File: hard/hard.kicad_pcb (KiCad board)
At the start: 2 copper layers, 125 parts, among them U1 STM32F401RETx, U2 USBLC6-2SC6, U3 AMS1117-3.3

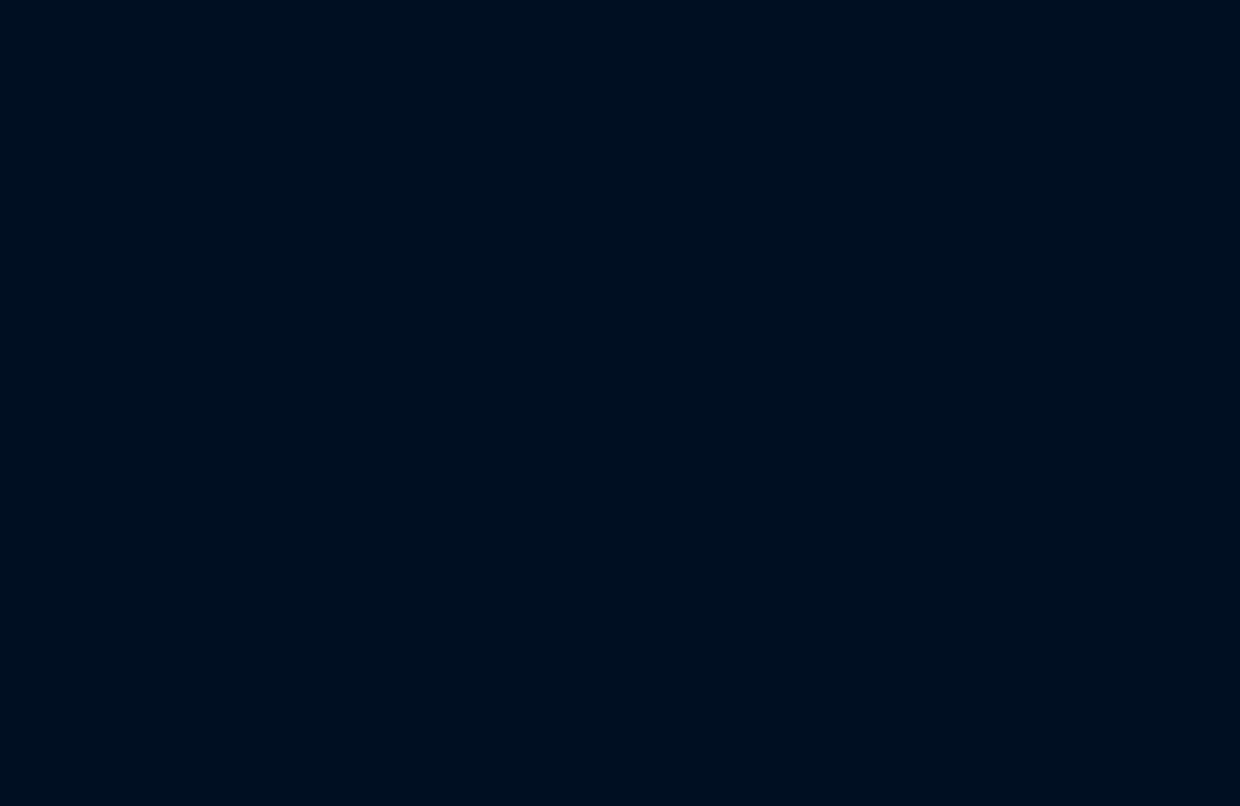
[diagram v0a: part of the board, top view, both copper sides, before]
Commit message: assign all footprints
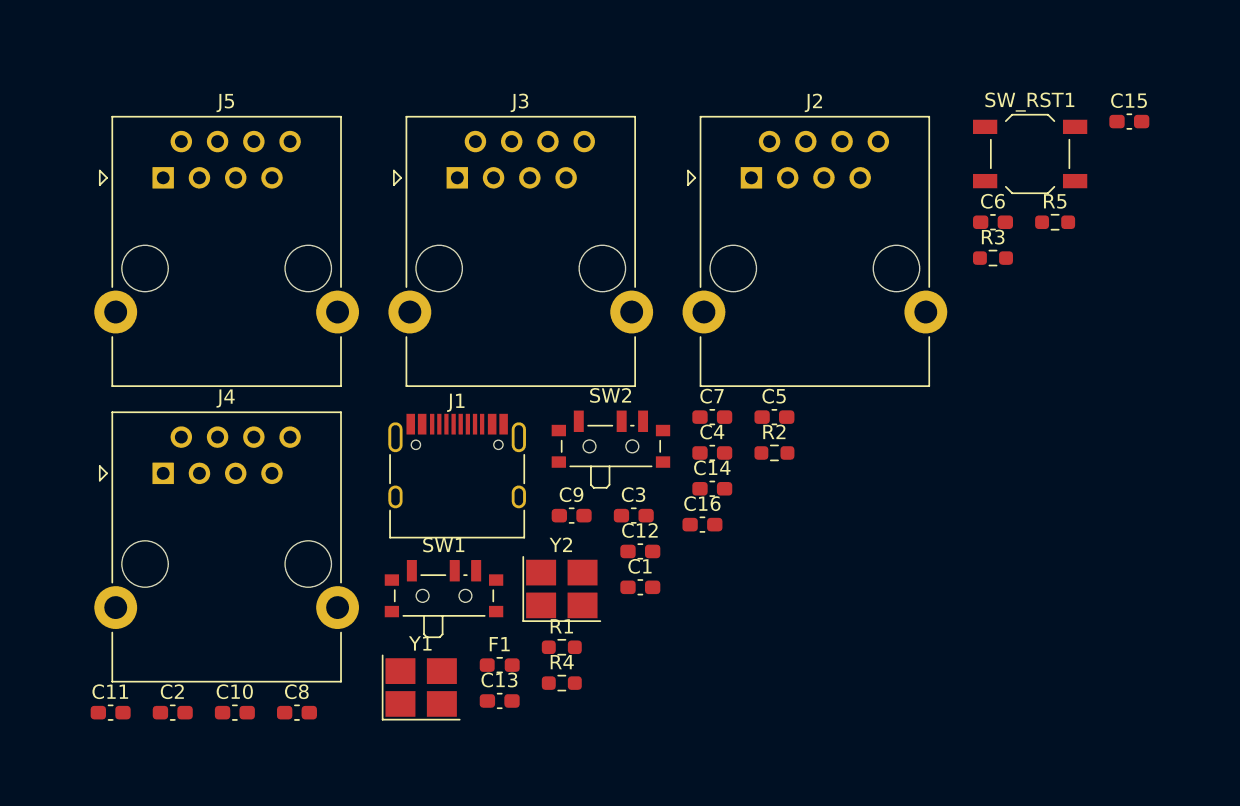
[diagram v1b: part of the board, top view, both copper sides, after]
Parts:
- added C1: 12pF, Capacitor_SMD:C_0603_1608Metric_Pad1.08x0.95mm_HandSolder, F.Cu at (949.3, -151.8)
- added C10: 0.1uF, Capacitor_SMD:C_0603_1608Metric_Pad1.08x0.95mm_HandSolder, F.Cu at (920.9, -143.0)
- added C11: 0.1uF, Capacitor_SMD:C_0603_1608Metric_Pad1.08x0.95mm_HandSolder, F.Cu at (912.2, -143.0)
- added C12: 0.1uF, Capacitor_SMD:C_0603_1608Metric_Pad1.08x0.95mm_HandSolder, F.Cu at (949.3, -154.3)
- added C13: 10uF, Capacitor_SMD:C_0603_1608Metric_Pad1.08x0.95mm_HandSolder, F.Cu at (939.5, -143.8)
- added C14: 0.1uF, Capacitor_SMD:C_0603_1608Metric_Pad1.08x0.95mm_HandSolder, F.Cu at (954.4, -158.7)
- added C15: 0.1uF, Capacitor_SMD:C_0603_1608Metric_Pad1.08x0.95mm_HandSolder, F.Cu at (983.6, -184.4)
- added C16: 10uF, Capacitor_SMD:C_0603_1608Metric_Pad1.08x0.95mm_HandSolder, F.Cu at (953.7, -156.2)
- added C2: 12pF, Capacitor_SMD:C_0603_1608Metric_Pad1.08x0.95mm_HandSolder, F.Cu at (916.6, -143.0)
- added C3: 12pF, Capacitor_SMD:C_0603_1608Metric_Pad1.08x0.95mm_HandSolder, F.Cu at (948.9, -156.8)
- added C4: 12pF, Capacitor_SMD:C_0603_1608Metric_Pad1.08x0.95mm_HandSolder, F.Cu at (954.4, -161.2)
- added C5: 0.1uF, Capacitor_SMD:C_0603_1608Metric_Pad1.08x0.95mm_HandSolder, F.Cu at (958.7, -163.7)
- added C6: 4.7uF, Capacitor_SMD:C_0603_1608Metric_Pad1.08x0.95mm_HandSolder, F.Cu at (974.0, -177.3)
- added C7: 0.1uF, Capacitor_SMD:C_0603_1608Metric_Pad1.08x0.95mm_HandSolder, F.Cu at (954.4, -163.7)
- added C8: 0.1uF, Capacitor_SMD:C_0603_1608Metric_Pad1.08x0.95mm_HandSolder, F.Cu at (925.3, -143.0)
- added C9: 0.1uF, Capacitor_SMD:C_0603_1608Metric_Pad1.08x0.95mm_HandSolder, F.Cu at (944.5, -156.8)
- added F1: Polyfuse, Fuse:Fuse_0603_1608Metric_Pad1.05x0.95mm_HandSolder, F.Cu at (939.5, -146.3)
- added J1: USB_C_Receptacle_USB2.0, Connector_USB:USB_C_Receptacle_HRO_TYPE-C-31-M-12, F.Cu at (936.5, -159.1)
- added J2: RJ45_Shielded, Connector_RJ:RJ45_Ninigi_GE, F.Cu at (957.1, -180.4)
- added J3: RJ45_Shielded, Connector_RJ:RJ45_Ninigi_GE, F.Cu at (936.5, -180.4)
- added J4: RJ45_Shielded, Connector_RJ:RJ45_Ninigi_GE, F.Cu at (915.9, -159.7)
- added J5: RJ45_Shielded, Connector_RJ:RJ45_Ninigi_GE, F.Cu at (915.9, -180.4)
- added R1: 10kohm, Resistor_SMD:R_0603_1608Metric_Pad0.98x0.95mm_HandSolder, F.Cu at (943.8, -147.6)
- added R2: 10kohm, Resistor_SMD:R_0603_1608Metric_Pad0.98x0.95mm_HandSolder, F.Cu at (958.7, -161.2)
- added R3: 4.7kohm, Resistor_SMD:R_0603_1608Metric_Pad0.98x0.95mm_HandSolder, F.Cu at (974.0, -174.8)
- added R4: 5.1kohm, Resistor_SMD:R_0603_1608Metric_Pad0.98x0.95mm_HandSolder, F.Cu at (943.8, -145.1)
- added R5: 5.1kohm, Resistor_SMD:R_0603_1608Metric_Pad0.98x0.95mm_HandSolder, F.Cu at (978.4, -177.3)
- added SW1: BOOT0, Button_Switch_SMD:SW_SPDT_PCM12, F.Cu at (935.6, -151.5)
- added SW2: BOOT1, Button_Switch_SMD:SW_SPDT_PCM12, F.Cu at (947.3, -162.0)
- added SW_RST1: RST, Button_Switch_SMD:SW_SPST_TL3342, F.Cu at (976.6, -182.1)
- added Y1: XTAL_8M, Crystal:Crystal_SMD_3225-4Pin_3.2x2.5mm_HandSoldering, F.Cu at (934.0, -144.7)
- added Y2: XTAL_8M, Crystal:Crystal_SMD_3225-4Pin_3.2x2.5mm_HandSoldering, F.Cu at (943.8, -151.6)
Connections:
- D62 pad 1: (no net) -> /COL7L
- U1 pad 28: (no net) -> /BOOT1
- U1 pad 3: (no net) -> /XTAL_32K_A
- U1 pad 30: (no net) -> Net-(C6-Pad1)
- U1 pad 4: (no net) -> /XTAL_32K_B
- U1 pad 60: (no net) -> /BOOT0
- U1 pad 7: (no net) -> Net-(R3-Pad2)
- U2 pad 4: (no net) -> Net-(J1-PadA7)
- U2 pad 6: (no net) -> Net-(J1-PadA6)
- U3 pad 3: (no net) -> Net-(C13-Pad1)

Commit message: draw outline
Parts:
- removed J4, J5: RJ45_Shielded, Connector_RJ:RJ45_Ninigi_GE
- added C17: 0.1uF, Capacitor_SMD:C_0603_1608Metric_Pad1.08x0.95mm_HandSolder, F.Cu at (1061.7, -113.0)
- added C18: 4.7uF, Capacitor_SMD:C_0603_1608Metric_Pad1.08x0.95mm_HandSolder, F.Cu at (1061.7, -110.5)
- added C19: 0.1uF, Capacitor_SMD:C_0603_1608Metric_Pad1.08x0.95mm_HandSolder, F.Cu at (1066.1, -113.0)
- added C20: 0.1uF, Capacitor_SMD:C_0603_1608Metric_Pad1.08x0.95mm_HandSolder, F.Cu at (1061.7, -108.0)
- added C21: 0.1uF, Capacitor_SMD:C_0603_1608Metric_Pad1.08x0.95mm_HandSolder, F.Cu at (1066.1, -110.5)
- added C22: 0.1uF, Capacitor_SMD:C_0603_1608Metric_Pad1.08x0.95mm_HandSolder, F.Cu at (1070.4, -113.0)
- added C23: 0.1uF, Capacitor_SMD:C_0603_1608Metric_Pad1.08x0.95mm_HandSolder, F.Cu at (1066.1, -108.0)
- added C24: 12pF, Capacitor_SMD:C_0603_1608Metric_Pad1.08x0.95mm_HandSolder, F.Cu at (1096.6, -132.7)
- added C25: 12pF, Capacitor_SMD:C_0603_1608Metric_Pad1.08x0.95mm_HandSolder, F.Cu at (1090.2, -125.8)
- added C26: 12pF, Capacitor_SMD:C_0603_1608Metric_Pad1.08x0.95mm_HandSolder, F.Cu at (1096.6, -130.2)
- added C27: 12pF, Capacitor_SMD:C_0603_1608Metric_Pad1.08x0.95mm_HandSolder, F.Cu at (1090.2, -123.3)
- added R6: 4.7kohm, Resistor_SMD:R_0603_1608Metric_Pad0.98x0.95mm_HandSolder, F.Cu at (1070.4, -110.5)
- added R7: 10kohm, Resistor_SMD:R_0603_1608Metric_Pad0.98x0.95mm_HandSolder, F.Cu at (1094.6, -125.8)
- added R8: 10kohm, Resistor_SMD:R_0603_1608Metric_Pad0.98x0.95mm_HandSolder, F.Cu at (1094.6, -123.3)
- added SW3: BOOT0, Button_Switch_SMD:SW_SPDT_PCM12, F.Cu at (1005.2, -87.6)
- added SW4: BOOT1, Button_Switch_SMD:SW_SPDT_PCM12, F.Cu at (1015.4, -87.6)
- added SW_RST2: RST, Button_Switch_SMD:SW_SPST_TL3342, F.Cu at (1048.4, -86.4)
- added U4: STM32F401RETx, Package_QFP:LQFP-64_10x10mm_P0.5mm, F.Cu at (1033.1, -80.6)
- added Y3: XTAL_8M, Crystal:Crystal_SMD_3225-4Pin_3.2x2.5mm_HandSoldering, F.Cu at (1078.1, -124.2)
- added Y4: XTAL_8M, Crystal:Crystal_SMD_3225-4Pin_3.2x2.5mm_HandSoldering, F.Cu at (1084.7, -124.2)
- SW_BS1: footprint hard:Kailh_Choc_V2_1.00u_PCB -> hard:Kailh_Choc_V2_1.50u_PCB
- moved U1 223.2 mm to (857.9, -81.9)
- moved SW_RST1 164.2 mm to (843.3, -86.4)
- moved J3 119.8 mm to (993.1, -74.9), turned to 180 degrees
- moved J2 113.4 mm to (915.7, -74.9), turned to 180 degrees
- moved SW2 97.7 mm to (883.9, -87.6), turned to 180 degrees
- moved D4 91.4 mm to (1016.4, -102.5)
- moved D10 91.4 mm to (1026.8, -114.4)
- moved D13 91.4 mm to (1008.8, -96.8)
- moved D15 91.4 mm to (1026.8, -117.0)
- moved D5 91.4 mm to (1026.8, -111.8)
- moved D11 91.4 mm to (1012.4, -99.9)
- moved D14 91.4 mm to (1012.4, -102.5)
- moved SW1 88.6 mm to (874.2, -87.6), turned to 180 degrees
- moved J1 84.5 mm to (894.7, -85.7), turned to 180 degrees
- moved D20 72.1 mm to (900.2, -149.4)
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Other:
- board outline added: 315.6 x 117.5 mm

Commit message: set all footprints
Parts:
- removed C26, C27, C3, C4: 12pF, Capacitor_SMD:C_0603_1608Metric_Pad1.08x0.95mm_HandSolder
- removed Y2, Y4: XTAL_8M, Crystal:Crystal_SMD_3225-4Pin_3.2x2.5mm_HandSoldering
- added REF**: MountingHole_2.2mm_M2, MountingHole:MountingHole_2.2mm_M2, F.Cu at (1037.6, -72.3)
- added REF**: MountingHole_2.2mm_M2, MountingHole:MountingHole_2.2mm_M2, F.Cu at (1037.6, -87.5)
- added REF**: MountingHole_2.2mm_M2, MountingHole:MountingHole_2.2mm_M2, F.Cu at (1001.4, -82.4)
- added REF**: MountingHole_2.2mm_M2, MountingHole:MountingHole_2.2mm_M2, F.Cu at (1001.4, -72.4)
- added REF**: MountingHole_2.2mm_M2, MountingHole:MountingHole_2.2mm_M2, F.Cu at (886.5, -72.5)
- added REF**: MountingHole_2.2mm_M2, MountingHole:MountingHole_2.2mm_M2, F.Cu at (886.5, -82.5)
- added REF**: MountingHole_2.2mm_M2, MountingHole:MountingHole_2.2mm_M2, F.Cu at (850.3, -72.5)
- added REF**: MountingHole_2.2mm_M2, MountingHole:MountingHole_2.2mm_M2, F.Cu at (850.3, -87.8)
- moved D61 239.2 mm to (1100.0, -10.2)
- moved D58 229.8 mm to (1106.2, -68.6)
- moved D36 227.3 mm to (996.3, 7.62)
- moved D49 217.3 mm to (1044.6, -10.8)
- moved D53 216.8 mm to (1054.1, -29.8)
- moved D4 214.7 mm to (822.3, -10.8)
- moved D60 212.9 mm to (1078.2, -29.2)
- moved D59 210.5 mm to (1085.8, -49.5)
- moved D52 206.6 mm to (1049.7, -48.9)
- moved D57 205.0 mm to (1062.4, -10.8)
- moved C22 204.9 mm to (869.3, -73.7), turned to 90 degrees
- moved D35 204.8 mm to (987.4, -11.4)
- moved D48 203.0 mm to (1035.0, -30.5)
- moved D5 202.3 mm to (829.3, -67.9)
- moved D56 201.9 mm to (1077.0, -67.3)
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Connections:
- C1 pad 1: /XTAL_8M_B -> /L_XTAL_8M_B
- C2 pad 1: /XTAL_8M_A -> /L_XTAL_8M_A
- C24 pad 1: /XTAL_8M_B -> /R_XTAL_8M_B
- C25 pad 1: /XTAL_8M_A -> /R_XTAL_8M_A
- D62 pad 1: /COL7L -> (no net)
- J2 pad 4: /ROW5L -> (no net)
- J2 pad 5: /ROW4L -> (no net)
- J2 pad 6: /ROW3L -> (no net)
- J2 pad 7: /ROW2L -> (no net)
- J2 pad 8: /ROW1L -> (no net)
- J3 pad 2: /COL7L -> (no net)
- J3 pad 3: /COL6L -> (no net)
- J3 pad 4: /COL5L -> (no net)
- J3 pad 5: /COL4L -> (no net)
- J3 pad 6: /COL3L -> (no net)
- J3 pad 7: /COL2L -> (no net)
- J3 pad 8: /COL1L -> (no net)
- R1 pad 1: /BOOT0 -> /R_BOOT0
- R2 pad 1: /BOOT1 -> /R_BOOT1
- R7 pad 1: /BOOT0 -> /L_BOOT0
- R8 pad 1: /BOOT1 -> /L_BOOT1
- SW1 pad 2: /BOOT0 -> /R_BOOT0
- SW2 pad 2: /BOOT1 -> /R_BOOT1
- SW3 pad 2: /BOOT0 -> /L_BOOT0
- SW4 pad 2: /BOOT1 -> /L_BOOT1
- U1 pad 28: /BOOT1 -> /L_BOOT1
- U1 pad 3: /XTAL_32K_A -> (no net)
- U1 pad 4: /XTAL_32K_B -> (no net)
- U1 pad 5: /XTAL_8M_A -> /L_XTAL_8M_A
- U1 pad 6: /XTAL_8M_A -> /L_XTAL_8M_B
- U1 pad 60: /BOOT0 -> /L_BOOT0
- U4 pad 28: /BOOT1 -> /R_BOOT1
- U4 pad 3: /XTAL_32K_A -> (no net)
- U4 pad 4: /XTAL_32K_B -> (no net)
- U4 pad 5: /XTAL_8M_A -> /R_XTAL_8M_A
- U4 pad 6: /XTAL_8M_A -> /R_XTAL_8M_B
- U4 pad 60: /BOOT0 -> /R_BOOT0
- Y1 pad 1: /XTAL_8M_B -> /L_XTAL_8M_B
- Y1 pad 3: /XTAL_8M_A -> /L_XTAL_8M_A
- Y3 pad 1: /XTAL_8M_B -> /R_XTAL_8M_B
- Y3 pad 3: /XTAL_8M_A -> /R_XTAL_8M_A
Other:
- outline, holes or cut-outs redrawn

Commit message: misc circuits
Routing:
- net +3V3: track 0.00 -> 2.33 mm
- net GND: track 0.00 -> 2.07 mm

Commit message: gen2
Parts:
- removed C15, C17, C19, C20, C21, C22, C23: 0.1uF, Capacitor_SMD:C_0603_1608Metric_Pad1.08x0.95mm_HandSolder
- removed C16: 10uF, Capacitor_SMD:C_0603_1608Metric_Pad1.08x0.95mm_HandSolder
- removed C18: 4.7uF, Capacitor_SMD:C_0603_1608Metric_Pad1.08x0.95mm_HandSolder
- removed C24, C25: 12pF, Capacitor_SMD:C_0603_1608Metric_Pad1.08x0.95mm_HandSolder
- removed D10, D11, D12, D13, D14, D15, D16, D17, D18, D19, D20, D21, D22, D23, D24, D25, D26, D27, D29, D30, D31, D32, D33, D34, D35, D36, D37, D38, D39, D4, D40, D41, D42, D43, D44, D45, D46, D47, D48, D49, D5, D50, D51, D52, D53, D54, D55, D56, D57, D58, D59, D6, D60, D61, D62, D7, D8, D9: D, Diode_SMD:D_0603_1608Metric
- removed J3: RJ45_Shielded, Connector_RJ:RJ45_Ninigi_GE
- removed REF** (x8): MountingHole_2.2mm_M2, MountingHole:MountingHole_2.2mm_M2
- removed SW_0: SW_0, hard:Kailh_Choc_V2_1.00u_PCB
- removed SW_1: SW_1, hard:Kailh_Choc_V2_1.00u_PCB
- removed SW_10: SW_6, hard:Kailh_Choc_V2_1.00u_PCB
- removed SW_2: SW_2, hard:Kailh_Choc_V2_1.00u_PCB
- removed SW_3: SW_3, hard:Kailh_Choc_V2_1.00u_PCB
- removed SW_4: SW_4, hard:Kailh_Choc_V2_1.00u_PCB
- removed SW_5: SW_5, hard:Kailh_Choc_V2_1.00u_PCB
- removed SW_7: SW_7, hard:Kailh_Choc_V2_1.00u_PCB
- removed SW_8: SW_8, hard:Kailh_Choc_V2_1.00u_PCB
- removed SW_9: SW_9, hard:Kailh_Choc_V2_1.00u_PCB
- removed SW_A1: SW_A, hard:Kailh_Choc_V2_1.00u_PCB
- removed SW_B1: SW_B, hard:Kailh_Choc_V2_1.00u_PCB
- removed SW_BQ1: SW_BQ, hard:Kailh_Choc_V2_1.00u_PCB
- removed SW_BS1: SW_BS, hard:Kailh_Choc_V2_1.50u_PCB
- removed SW_C1: SW_C, hard:Kailh_Choc_V2_1.00u_PCB
- removed SW_CMM1: SW_CMM, hard:Kailh_Choc_V2_1.00u_PCB
- removed SW_CTRL1: SW_CTRL, hard:Kailh_Choc_V2_1.75u_PCB
- removed SW_D1: SW_D, hard:Kailh_Choc_V2_1.00u_PCB
- removed SW_DEL1: SW_DEL, hard:Kailh_Choc_V2_2.00u_PCB
- removed SW_E1: SW_E, hard:Kailh_Choc_V2_1.00u_PCB
- removed SW_ESC1: SW_ESC, hard:Kailh_Choc_V2_1.00u_PCB
- removed SW_F1: SW_F, hard:Kailh_Choc_V2_1.00u_PCB
- removed SW_FN1: SW_FN, hard:Kailh_Choc_V2_1.00u_PCB
- removed SW_G1: SW_G, hard:Kailh_Choc_V2_1.00u_PCB
- removed SW_H1: SW_H, hard:Kailh_Choc_V2_1.00u_PCB
- removed SW_HYPH1: SW_HYPH, hard:Kailh_Choc_V2_1.00u_PCB
- removed SW_I1: SW_I, hard:Kailh_Choc_V2_1.00u_PCB
- removed SW_J1: SW_J, hard:Kailh_Choc_V2_1.00u_PCB
- removed SW_K1: SW_K, hard:Kailh_Choc_V2_1.00u_PCB
- removed SW_L1: SW_L, hard:Kailh_Choc_V2_1.00u_PCB
- removed SW_LALT1: SW_LALT, hard:Kailh_Choc_V2_1.25u_PCB
- removed SW_LB1: SW_LB, hard:Kailh_Choc_V2_1.00u_PCB
- removed SW_LCMD1: SW_LCMD, hard:Kailh_Choc_V2_1.25u_PCB
- removed SW_LSFT1: SW_LSFT, hard:Kailh_Choc_V2_2.25u_PCB
- removed SW_LSPC1: SW_LSPC, hard:Kailh_Choc_V2_2.00u_PCB
- removed SW_M1: SW_M, hard:Kailh_Choc_V2_1.00u_PCB
- removed SW_N1: SW_N, hard:Kailh_Choc_V2_1.00u_PCB
- removed SW_O1: SW_O, hard:Kailh_Choc_V2_1.00u_PCB
- removed SW_P1: SW_P, hard:Kailh_Choc_V2_1.00u_PCB
- removed SW_PLUS1: SW_PLUS, hard:Kailh_Choc_V2_1.00u_PCB
- removed SW_PRD1: SW_PRD, hard:Kailh_Choc_V2_1.00u_PCB
- removed SW_Q1: SW_Q, hard:Kailh_Choc_V2_1.00u_PCB
- removed SW_R1: SW_R, hard:Kailh_Choc_V2_1.00u_PCB
- removed SW_RALT1: SW_RALT, hard:Kailh_Choc_V2_1.25u_PCB
- removed SW_RB1: SW_RB, hard:Kailh_Choc_V2_1.00u_PCB
- removed SW_RCMD1: SW_RCMD, hard:Kailh_Choc_V2_1.25u_PCB
- removed SW_RET1: SW_RET, hard:Kailh_Choc_V2_2.75u_PCB
- removed SW_RSFT1: SW_RSFT, hard:Kailh_Choc_V2_2.25u_PCB
- removed SW_RSPC1: SW_RSPC, hard:Kailh_Choc_V2_2.00u_PCB
- removed SW_RST1, SW_RST2: RST, Button_Switch_SMD:SW_SPST_TL3342
- removed SW_S1: SW_S, hard:Kailh_Choc_V2_1.00u_PCB
- removed SW_SEMI1: SW_SEMI, hard:Kailh_Choc_V2_1.00u_PCB
- removed SW_SLA1: SW_SLA, hard:Kailh_Choc_V2_1.00u_PCB
- removed SW_SQ1: SW_SQ, hard:Kailh_Choc_V2_1.00u_PCB
- removed SW_T1: SW_T, hard:Kailh_Choc_V2_1.00u_PCB
- removed SW_TAB1: SW_TAB, hard:Kailh_Choc_V2_1.50u_PCB
- removed SW_U1: SW_U, hard:Kailh_Choc_V2_1.00u_PCB
- removed SW_V1: SW_V, hard:Kailh_Choc_V2_1.00u_PCB
- removed SW_W1: SW_W, hard:Kailh_Choc_V2_1.00u_PCB
- removed SW_X1: SW_X, hard:Kailh_Choc_V2_1.00u_PCB
- removed SW_Y1: SW_Y, hard:Kailh_Choc_V2_1.00u_PCB
- removed SW_Z1: SW_Z, hard:Kailh_Choc_V2_1.00u_PCB
- removed Y3: XTAL_8M, Crystal:Crystal_SMD_3225-4Pin_3.2x2.5mm_HandSoldering
- added C3: 0.1uF, Capacitor_SMD:C_0402_1005Metric_Pad0.74x0.62mm_HandSolder, F.Cu at (175.8, 64.0)
- added C4: 0.1uF, Capacitor_SMD:C_0402_1005Metric_Pad0.74x0.62mm_HandSolder, F.Cu at (181.6, 63.0)
- added R10: 330Ohm, Resistor_SMD:R_0402_1005Metric_Pad0.72x0.64mm_HandSolder, F.Cu at (168.3, 45.7)
- added R9: 330Ohm, Resistor_SMD:R_0402_1005Metric_Pad0.72x0.64mm_HandSolder, F.Cu at (165.1, 46.4)
- added REF_M1: MountingHole_2.2mm_M2_DIN965, MountingHole:MountingHole_2.2mm_M2_DIN965, F.Cu at (188.0, 48.3)
- added REF_M2: MountingHole_2.2mm_M2_DIN965, MountingHole:MountingHole_2.2mm_M2_DIN965, F.Cu at (188.0, 62.9)
- added REF_M3: MountingHole_2.2mm_M2_DIN965, MountingHole:MountingHole_2.2mm_M2_DIN965, F.Cu at (153.0, 48.3)
- added REF_M4: MountingHole_2.2mm_M2_DIN965, MountingHole:MountingHole_2.2mm_M2_DIN965, F.Cu at (153.0, 62.9)
- added SW10: KEY_Q, hard:Kailh_Choc_V2_1.00u_PCB, F.Cu at (120.0, 89.5)
- added SW11: KEY_A, hard:Kailh_Choc_V2_1.00u_PCB, F.Cu at (125.3, 108.6)
- added SW12: KEY_OPTION, hard:Kailh_Choc_V2_1.25u_PCB, F.Cu at (136.7, 146.7)
- added SW13: KEY_2, hard:Kailh_Choc_V2_1.00u_PCB, F.Cu at (129.5, 70.5)
- added SW14: KEY_Z, hard:Kailh_Choc_V2_1.00u_PCB, F.Cu at (134.3, 127.6)
- added SW15: KEY_W, hard:Kailh_Choc_V2_1.00u_PCB, F.Cu at (139.1, 89.5)
- added SW16: KEY_S, hard:Kailh_Choc_V2_1.00u_PCB, F.Cu at (144.3, 108.6)
- added SW17: KEY_COMMAND, hard:Kailh_Choc_V2_1.25u_PCB, F.Cu at (160.5, 146.7)
- added SW18: KEY_3, hard:Kailh_Choc_V2_1.00u_PCB, F.Cu at (148.6, 70.5)
- added SW19: KEY_X, hard:Kailh_Choc_V2_1.00u_PCB, F.Cu at (153.4, 127.6)
- added SW20: KEY_E, hard:Kailh_Choc_V2_1.00u_PCB, F.Cu at (158.1, 89.5)
- added SW21: KEY_D, hard:Kailh_Choc_V2_1.00u_PCB, F.Cu at (163.4, 108.6)
- added SW22: KEY_4, hard:Kailh_Choc_V2_1.00u_PCB, F.Cu at (167.6, 70.5)
- added SW23: KEY_C, hard:Kailh_Choc_V2_1.00u_PCB, F.Cu at (172.4, 127.6)
- added SW24: KEY_R, hard:Kailh_Choc_V2_1.00u_PCB, F.Cu at (177.2, 89.5)
- added SW25: KEY_F, hard:Kailh_Choc_V2_1.00u_PCB, F.Cu at (182.4, 108.6)
- added SW26: KEY_5, hard:Kailh_Choc_V2_1.00u_PCB, F.Cu at (186.7, 70.5)
- added SW27: KEY_SPACE, hard:Kailh_Choc_V2_2.00u_PCB, F.Cu at (195.6, 146.7)
- added SW28: KEY_V, hard:Kailh_Choc_V2_1.00u_PCB, F.Cu at (191.5, 127.6)
- added SW29: KEY_T, hard:Kailh_Choc_V2_1.00u_PCB, F.Cu at (196.2, 89.5)
- added SW30: KEY_G, hard:Kailh_Choc_V2_1.00u_PCB, F.Cu at (201.5, 108.6)
- added SW31: KEY_6, hard:Kailh_Choc_V2_1.00u_PCB, F.Cu at (205.7, 70.5)
- added SW32: KEY_B, hard:Kailh_Choc_V2_1.00u_PCB, F.Cu at (210.5, 127.6)
- added SW5: KEY_LFN, hard:Kailh_Choc_V2_1.00u_PCB, F.Cu at (91.5, 146.7)
- added SW6: KEY_TAB, hard:Kailh_Choc_V2_1.50u_PCB, F.Cu at (96.2, 89.5)
- added SW7: KEY_ESCAPE, hard:Kailh_Choc_V2_1.00u_PCB, F.Cu at (91.4, 70.5)
- added SW8: KEY_CONTROL, hard:Kailh_Choc_V2_1.25u_PCB, F.Cu at (112.9, 146.7)
- added SW9: KEY_1, hard:Kailh_Choc_V2_1.00u_PCB, F.Cu at (110.5, 70.5)
- added U5: STM32L412RBTx, Package_QFP:LQFP-64_10x10mm_P0.5mm, F.Cu at (164.7, 55.4)
- C1: value 12pF -> 0.1uF; footprint Capacitor_SMD:C_0603_1608Metric_Pad1.08x0.95mm_HandSolder -> Capacitor_SMD:C_0402_1005Metric_Pad0.74x0.62mm_HandSolder
- C10, C11, C12, C14, C8, C9: footprint Capacitor_SMD:C_0603_1608Metric_Pad1.08x0.95mm_HandSolder -> Capacitor_SMD:C_0402_1005Metric_Pad0.74x0.62mm_HandSolder
- C13: value 10uF -> 0.1uF; footprint Capacitor_SMD:C_0603_1608Metric_Pad1.08x0.95mm_HandSolder -> Capacitor_SMD:C_0402_1005Metric_Pad0.74x0.62mm_HandSolder
- C2: value 12pF -> 1uF
- C5: value 0.1uF -> 1uF
- C6: value 4.7uF -> 10pF; footprint Capacitor_SMD:C_0603_1608Metric_Pad1.08x0.95mm_HandSolder -> Capacitor_SMD:C_0402_1005Metric_Pad0.74x0.62mm_HandSolder
- C7: value 0.1uF -> 10pF; footprint Capacitor_SMD:C_0603_1608Metric_Pad1.08x0.95mm_HandSolder -> Capacitor_SMD:C_0402_1005Metric_Pad0.74x0.62mm_HandSolder
- D1: footprint Diode_SMD:D_0603_1608Metric -> Diode_SMD:D_SOD-123
- D2: value D -> STATUS1; footprint Diode_SMD:D_0603_1608Metric -> LED_SMD:LED_0603_1608Metric_Pad1.05x0.95mm_HandSolder
- D3: value D -> STATUS2; footprint Diode_SMD:D_0603_1608Metric -> LED_SMD:LED_0603_1608Metric_Pad1.05x0.95mm_HandSolder
- F1: footprint Fuse:Fuse_0603_1608Metric_Pad1.05x0.95mm_HandSolder -> Fuse:Fuse_0805_2012Metric_Pad1.15x1.40mm_HandSolder
- J2: value RJ45_Shielded -> RJ45_LED_Shielded; footprint Connector_RJ:RJ45_Ninigi_GE -> Connector_RJ:RJ45_Hanrun_HR911105A
- R1, R2: value 10kohm -> 5.1kOhm; footprint Resistor_SMD:R_0603_1608Metric_Pad0.98x0.95mm_HandSolder -> Resistor_SMD:R_0402_1005Metric_Pad0.72x0.64mm_HandSolder
- R3: value 4.7kohm -> R; footprint Resistor_SMD:R_0603_1608Metric_Pad0.98x0.95mm_HandSolder -> Resistor_SMD:R_0402_1005Metric_Pad0.72x0.64mm_HandSolder
- R4: value 5.1kohm -> R; footprint Resistor_SMD:R_0603_1608Metric_Pad0.98x0.95mm_HandSolder -> Resistor_SMD:R_0402_1005Metric_Pad0.72x0.64mm_HandSolder
- R5: value 5.1kohm -> 4.7kOhm; footprint Resistor_SMD:R_0603_1608Metric_Pad0.98x0.95mm_HandSolder -> Resistor_SMD:R_0402_1005Metric_Pad0.72x0.64mm_HandSolder
- R6: value 4.7kohm -> 4.7kOhm; footprint Resistor_SMD:R_0603_1608Metric_Pad0.98x0.95mm_HandSolder -> Resistor_SMD:R_0402_1005Metric_Pad0.72x0.64mm_HandSolder
- R7: value 10kohm -> 2.2kOhm; footprint Resistor_SMD:R_0603_1608Metric_Pad0.98x0.95mm_HandSolder -> Resistor_SMD:R_0402_1005Metric_Pad0.72x0.64mm_HandSolder
- R8: value 10kohm -> 3.3kOhm; footprint Resistor_SMD:R_0603_1608Metric_Pad0.98x0.95mm_HandSolder -> Resistor_SMD:R_0402_1005Metric_Pad0.72x0.64mm_HandSolder
- SW1: value BOOT0 -> SW_RST; footprint Button_Switch_SMD:SW_SPDT_PCM12 -> Button_Switch_SMD:SW_SPST_CK_KXT3
- SW2: value BOOT1 -> SW_BOOT0; footprint Button_Switch_SMD:SW_SPDT_PCM12 -> Button_Switch_SMD:SW_SPST_CK_KXT3
- SW3: value BOOT0 -> KEY_CAPSLOCK; footprint Button_Switch_SMD:SW_SPDT_PCM12 -> hard:Kailh_Choc_V2_1.75u_PCB
- SW4: value BOOT1 -> KEY_LSHIFT; footprint Button_Switch_SMD:SW_SPDT_PCM12 -> hard:Kailh_Choc_V2_2.25u_PCB
- U1: value STM32F401RETx -> THVD1451D; footprint Package_QFP:LQFP-64_10x10mm_P0.5mm -> Package_SO:SOIC-8_3.9x4.9mm_P1.27mm
- U3: value AMS1117-3.3 -> MIC5504-3.3YM5; footprint Package_TO_SOT_SMD:SOT-223-3_TabPin2 -> Package_TO_SOT_SMD:SOT-23-5
- U4: value STM32F401RETx -> STLinkV3; footprint Package_QFP:LQFP-64_10x10mm_P0.5mm -> hard:IDC-Header_2x07_P1.27mm_Vertical
- Y1: value XTAL_8M -> 8MHz
- moved SW4 937.1 mm to (103.4, 127.6), turned to 0 degrees
- moved SW3 927.6 mm to (98.6, 108.6), turned to 0 degrees
- moved R6 894.3 mm to (158.1, 48.3)
- moved U4 886.1 mm to (148.6, 62.1)
- moved C5 854.3 mm to (183.1, 63.0), turned to 270 degrees
- moved R8 842.4 mm to (186.1, 60.3)
- moved R7 834.9 mm to (183.5, 60.3)
- moved R5 749.9 mm to (158.1, 47.0)
- moved SW2 748.8 mm to (148.0, 50.2), turned to 0 degrees
- moved SW1 738.7 mm to (148.0, 47.6), turned to 0 degrees
- moved C7 737.6 mm to (153.5, 59.7), turned to 180 degrees
- moved C13 733.6 mm to (157.9, 51.3), turned to 225 degrees
- moved J2 732.5 mm to (195.6, 59.4), turned to 90 degrees
- moved Y1 731.8 mm to (153.5, 56.3)
- moved J1 729.0 mm to (178.3, 49.3)
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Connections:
- net +5V renamed Net-(F1-Pad2)
- C1 pad 1: /L_XTAL_8M_B -> +3V3
- C13 pad 1: Net-(C13-Pad1) -> GND
- C13 pad 2: GND -> +3V3
- C14 pad 1: Net-(C13-Pad1) -> /V_SHARED
- C2 pad 1: /L_XTAL_8M_A -> Net-(C2-Pad1)
- C6 pad 1: Net-(C6-Pad1) -> /XTAL_A
- C7 pad 1: GND -> /XTAL_B
- C7 pad 2: +3V3 -> GND
- D1 pad 1: /COL1L -> Net-(C2-Pad1)
- D1 pad 2: Net-(D1-Pad2) -> /V_SHARED
- D2 pad 1: /COL1L -> Net-(D2-Pad1)
- D3 pad 1: /COL1L -> Net-(D3-Pad1)
- F1 pad 1: Net-(C13-Pad1) -> /V_SHARED
- J2 pad 1: (no net) -> /ETH_TX-
- J2 pad 2: (no net) -> /ETH_TX+
- J2 pad 3: (no net) -> /ETH_RX-
- J2 pad 4: (no net) -> /V_SHARED
- J2 pad 5: (no net) -> /V_SHARED
- J2 pad 6: (no net) -> /ETH_RX+
- J2 pad 7: (no net) -> GND
- J2 pad 8: (no net) -> GND
- R1 pad 1: /R_BOOT0 -> Net-(J1-PadB5)
- R2 pad 1: /R_BOOT1 -> Net-(J1-PadA5)
- R3 pad 1: +3V3 -> GND
- R3 pad 2: Net-(R3-Pad2) -> Net-(J2-Pad9)
- R4 pad 1: Net-(J1-PadB5) -> GND
- R4 pad 2: GND -> Net-(J2-Pad11)
- R5 pad 1: Net-(J1-PadA5) -> +3V3
- R5 pad 2: GND -> /NRST
- R6 pad 1: +3V3 -> Net-(R6-Pad1)
- R6 pad 2: Net-(R6-Pad2) -> GND
- R7 pad 1: /L_BOOT0 -> Net-(C2-Pad1)
- R7 pad 2: GND -> /VBUS_DETECT
- R8 pad 1: /L_BOOT1 -> /VBUS_DETECT
- SW1 pad 2: /R_BOOT0 -> /NRST
- SW2 pad 1: GND -> +3V3
- SW2 pad 2: /R_BOOT1 -> Net-(R6-Pad1)
- SW3 pad 2: /L_BOOT0 -> /KEY_CAPSLOCK
- SW4 pad 2: /L_BOOT1 -> /KEY_LSHIFT
- U1 pad 2: (no net) -> /RX
- U1 pad 3: (no net) -> /TX
- U1 pad 4: (no net) -> GND
- U1 pad 5: /L_XTAL_8M_A -> /ETH_TX-
- U1 pad 6: /L_XTAL_8M_B -> /ETH_TX+
- U1 pad 7: Net-(R3-Pad2) -> /ETH_RX-
- U1 pad 8: (no net) -> /ETH_RX+
- U2 pad 1: (no net) -> /D+
- U2 pad 3: (no net) -> /D-
- U2 pad 5: +3V3 -> /V_SHARED
- U3 pad 1: GND -> Net-(C2-Pad1)
- U3 pad 2: +3V3 -> GND
- U3 pad 3: Net-(C13-Pad1) -> Net-(C2-Pad1)
- U4 pad 1: +3V3 -> (no net)
- U4 pad 10: (no net) -> /JTDI
- U4 pad 11: (no net) -> GND
- U4 pad 12: GND -> /NRST
- U4 pad 13: +3V3 -> /VPC_TX
- U4 pad 14: (no net) -> /VPC_RX
- U4 pad 3: (no net) -> +3V3
- U4 pad 4: (no net) -> /JTMS
- U4 pad 5: /R_XTAL_8M_A -> GND
- U4 pad 6: /R_XTAL_8M_B -> /JTCK
- U4 pad 7: Net-(R6-Pad2) -> GND
- U4 pad 8: (no net) -> /JTDO
- U4 pad 9: (no net) -> /JTCK
- Y1 pad 1: /L_XTAL_8M_B -> /XTAL_A
- Y1 pad 3: /L_XTAL_8M_A -> /XTAL_B
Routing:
- net GND: track 2.07 -> 214.1 mm, vias 0 -> 12
- net /KEY_LFN: track 0.00 -> 129.3 mm, vias 0 -> 1
- net /KEY_B: track 0.00 -> 123.1 mm, vias 0 -> 1
- net /KEY_CONTROL: track 0.00 -> 119.2 mm, vias 0 -> 1
- net /KEY_SPACE: track 0.00 -> 114.3 mm, vias 0 -> 1
- net /KEY_OPTION: track 0.00 -> 114.3 mm, vias 0 -> 1
- net +3V3: track 2.33 -> 115.7 mm, vias 0 -> 10
- net /KEY_V: track 0.00 -> 109.1 mm, vias 0 -> 1
- net /KEY_CAPSLOCK: track 0.00 -> 102.6 mm
- net /KEY_Q: track 0.00 -> 101.6 mm, vias 0 -> 2
- net /KEY_COMMAND: track 0.00 -> 100.8 mm, vias 0 -> 1
- net /KEY_G: track 0.00 -> 97.6 mm, vias 0 -> 1
- net /KEY_A: track 0.00 -> 94.6 mm, vias 0 -> 4
- net /KEY_X: track 0.00 -> 90.9 mm, vias 0 -> 2
- net /KEY_C: track 0.00 -> 90.9 mm, vias 0 -> 3
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- added copper zone on B.Cu, net GND
- added copper zone on F.Cu, net GND
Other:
- board size 315.6 x 117.5 mm -> 138.1 x 118.7 mm
- net class Default: trace_width 0.25 -> 0.2; via_dia 0.8 -> 0.5; via_drill 0.4 -> 0.3

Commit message: cannot connect
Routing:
- net GND: track 214.1 -> 0.00 mm, vias 12 -> 0
- net /KEY_LFN: track 129.3 -> 0.00 mm, vias 1 -> 0
- net /KEY_B: track 123.1 -> 0.00 mm, vias 1 -> 0
- net /KEY_CONTROL: track 119.2 -> 0.00 mm, vias 1 -> 0
- net +3V3: track 115.7 -> 0.00 mm, vias 10 -> 0
- net /KEY_SPACE: track 114.3 -> 0.00 mm, vias 1 -> 0
- net /KEY_OPTION: track 114.3 -> 0.00 mm, vias 1 -> 0
- net /KEY_V: track 109.1 -> 0.00 mm, vias 1 -> 0
- net /KEY_CAPSLOCK: track 102.6 -> 0.00 mm
- net /KEY_Q: track 101.6 -> 0.00 mm, vias 2 -> 0
- net /KEY_COMMAND: track 100.8 -> 0.00 mm, vias 1 -> 0
- net /KEY_G: track 97.6 -> 0.00 mm, vias 1 -> 0
- net /KEY_A: track 94.6 -> 0.00 mm, vias 4 -> 0
- net /KEY_X: track 90.9 -> 0.00 mm, vias 2 -> 0
- net /KEY_C: track 90.9 -> 0.00 mm, vias 3 -> 0
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
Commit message: hard: new shape
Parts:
- U1: value THVD1451D -> LTC2852xMS; footprint Package_SO:SOIC-8_3.9x4.9mm_P1.27mm -> Package_SO:MSOP-10_3x3mm_P0.5mm
- moved REF_M3 107.5 mm to (233.0, 120.0)
- moved SW1 103.6 mm to (232.7, 107.3), turned to 180 degrees
- moved SW2 100.8 mm to (232.7, 104.8), turned to 180 degrees
- moved U4 88.9 mm to (232.0, 92.8), turned to 0 degrees
- moved C7 84.6 mm to (222.4, 108.9), turned to 270 degrees
- moved Y1 84.0 mm to (218.9, 108.9), turned to 0 degrees
- moved C6 83.6 mm to (215.4, 108.9), turned to 90 degrees
- moved J2 82.4 mm to (222.6, 137.3)
- moved R5 82.0 mm to (220.2, 100.6), turned to 225 degrees
- moved REF_M4 81.7 mm to (211.5, 120.0)
- moved C13 77.8 mm to (219.7, 98.5), turned to 45 degrees
- moved C11 76.9 mm to (215.3, 102.9), turned to 45 degrees
- moved C1 75.8 mm to (221.6, 119.3), turned to 90 degrees
- moved R9 72.0 mm to (223.1, 89.0), turned to 270 degrees
- moved R6 71.9 mm to (205.4, 102.5), turned to 270 degrees
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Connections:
- C14 pad 1: /V_SHARED -> Net-(C14-Pad1)
- C2 pad 1: Net-(C2-Pad1) -> /V_SHARED
- C3 pad 1: Net-(C2-Pad1) -> /V_SHARED
- D1 pad 1: Net-(C2-Pad1) -> /V_SHARED
- D1 pad 2: /V_SHARED -> Net-(C14-Pad1)
- F1 pad 1: /V_SHARED -> Net-(C14-Pad1)
- J1 pad A8: (no net) -> Net-(J1-PadA8)
- J1 pad B8: (no net) -> Net-(J1-PadB8)
- R7 pad 1: Net-(C2-Pad1) -> Net-(C14-Pad1)
- U1 pad 1: +3V3 -> /RX
- U1 pad 2: /RX -> GND
- U1 pad 3: /TX -> +3V3
- U1 pad 4: GND -> /TX
- U1 pad 5: /ETH_TX- -> GND
- U1 pad 6: /ETH_TX+ -> /ETH_TX-
- U1 pad 7: /ETH_RX- -> /ETH_TX+
- U1 pad 8: /ETH_RX+ -> /ETH_RX-
- U2 pad 5: /V_SHARED -> Net-(C14-Pad1)
- U3 pad 1: Net-(C2-Pad1) -> /V_SHARED
- U3 pad 3: Net-(C2-Pad1) -> /V_SHARED
- U3 pad 4: (no net) -> Net-(U3-Pad4)
- U4 pad 1: (no net) -> Net-(U4-Pad1)
- U4 pad 2: (no net) -> Net-(U4-Pad2)
- U5 pad 14: (no net) -> Net-(U5-Pad14)
- U5 pad 15: (no net) -> Net-(U5-Pad15)
- U5 pad 30: (no net) -> Net-(U5-Pad30)
- U5 pad 4: (no net) -> Net-(U5-Pad4)
- U5 pad 61: (no net) -> Net-(U5-Pad61)
- U5 pad 62: (no net) -> Net-(U5-Pad62)
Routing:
- removed copper zone on B.Cu, net GND
- removed copper zone on F.Cu, net GND
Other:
- board size 138.1 x 118.7 mm -> 156.2 x 97.2 mm
